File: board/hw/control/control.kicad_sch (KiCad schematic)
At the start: 25 parts, among them J1 stepper #1, J2 stepper #2, J3 buttons, J4 power, J6 AVR-ISP-10, U1 ULN2003A, U2 ULN2003A, U3 ULN2003A, U4 ULN2003A, U5 LM78L05_SO8

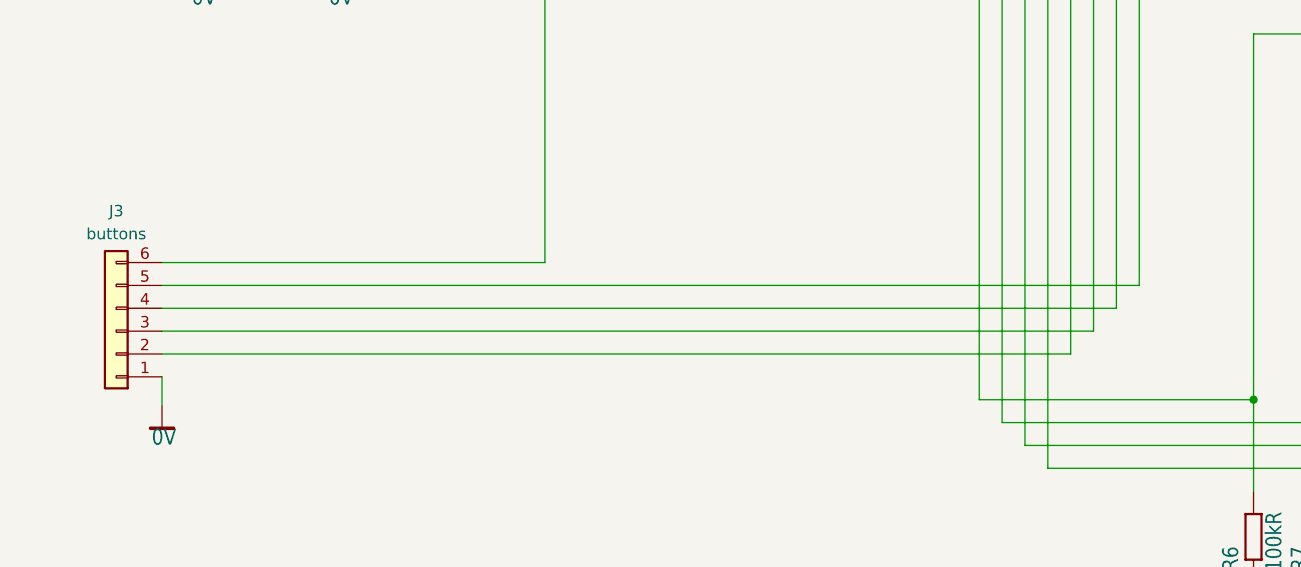
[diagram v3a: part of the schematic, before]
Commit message: assigned correct sizes of elements + some draft positioning; still need to add power management cirtcuitry
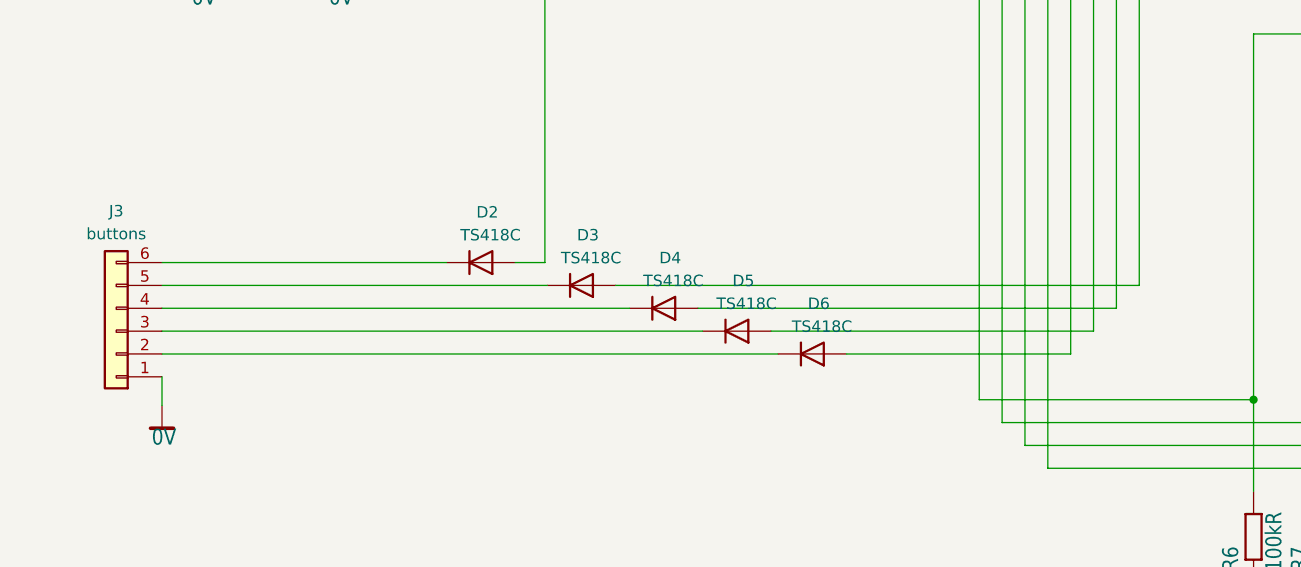
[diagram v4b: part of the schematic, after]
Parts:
- added D2, D3, D4, D5, D6: TS418C, Diode_SMD:D_0805_2012Metric, symbol Diode:CD4148W
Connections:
- net at J3.2 (Pin_2): now also D6.1 (K); no longer U$1.8 ((T0)PD4)
- net at J3.3 (Pin_3): now also D5.1 (K); no longer U$1.9 ((T1)PD5)
- net at J3.4 (Pin_4): now also D4.1 (K); no longer U$1.11 ((ICP)PD6)
- net at J3.5 (Pin_5): now also D3.1 (K); no longer U$1.16 ((OC1B)PB4)
- net at J3.6 (Pin_6): now also D2.1 (K); no longer U$1.5 (PA0(XTAL1))
- new net: D3.2 (A), U$1.16 ((OC1B)PB4)
- new net: D6.2 (A), U$1.8 ((T0)PD4)
- new net: D2.2 (A), U$1.5 (PA0(XTAL1))
- new net: D4.2 (A), U$1.11 ((ICP)PD6)
- new net: D5.2 (A), U$1.9 ((T1)PD5)
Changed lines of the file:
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@@
+    (stroke (width 0) (type default))
+  )
+  (wire (pts (xy 77.978 142.24) (xy 81.28 142.24))
     (stroke (width 0) (type default))
   )
@@
     (stroke (width 0) (type default))
   )
+  (wire (pts (xy 89.154 144.78) (xy 147.32 144.78))
+    (stroke (width 0) (type default))
+  )
   (wire (pts (xy 240.03 81.28) (xy 246.38 81.28))
     (stroke (width 0) (type default))
@@
     (stroke (width 0) (type default))
   )
+  (wire (pts (xy 114.808 152.4) (xy 139.7 152.4))
+    (stroke (width 0) (type default))
+  )
   (wire (pts (xy 257.81 116.84) (xy 245.11 116.84))
     (stroke (width 0) (type default))
@@
     (stroke (width 0) (type default))
   )
+  (wire (pts (xy 106.426 149.86) (xy 142.24 149.86))
+    (stroke (width 0) (type default))
+  )
   (wire (pts (xy 88.9 88.9) (xy 81.28 88.9))
     (stroke (width 0) (type default))
@@
     (stroke (width 0) (type default))
   )
+  (wire (pts (xy 38.735 144.78) (xy 81.534 144.78))
+    (stroke (width 0) (type default))
+  )
   (wire (pts (xy 160.02 167.64) (xy 160.02 157.48))
     (stroke (width 0) (type default))
@@
     (stroke (width 0) (type default))
   )
+  (wire (pts (xy 38.735 142.24) (xy 70.358 142.24))
+    (stroke (width 0) (type default))
+  )
   (wire (pts (xy 213.36 116.84) (xy 160.02 116.84))
     (stroke (width 0) (type default))
@@
     (stroke (width 0) (type default))
   )
-  (wire (pts (xy 38.735 144.78) (xy 147.32 144.78))
-    (stroke (width 0) (type default))
-  )
   (wire (pts (xy 38.735 154.94) (xy 38.735 158.115))
     (stroke (width 0) (type default))
@@
     (stroke (width 0) (type default))
   )
-  (wire (pts (xy 38.735 152.4) (xy 139.7 152.4))
-    (stroke (width 0) (type default))
-  )
   (wire (pts (xy 213.36 127) (xy 213.36 129.54))
     (stroke (width 0) (type default))
@@
     (stroke (width 0) (type default))
   )
+  (wire (pts (xy 98.298 147.32) (xy 144.78 147.32))
+    (stroke (width 0) (type default))
+  )
   (wire (pts (xy 147.32 71.12) (xy 147.32 144.78))
     (stroke (width 0) (type default))
@@
     (stroke (width 0) (type default))
   )
-  (wire (pts (xy 38.735 147.32) (xy 144.78 147.32))
-    (stroke (width 0) (type default))
-  )
   (wire (pts (xy 213.36 76.2) (xy 185.42 76.2))
     (stroke (width 0) (type default))
   )
-  (wire (pts (xy 38.735 149.86) (xy 142.24 149.86))
-    (stroke (width 0) (type default))
-  )
   (wire (pts (xy 219.71 119.38) (xy 213.36 119.38))
     (stroke (width 0) (type default))
@@
     (stroke (width 0) (type default))
   )
+  (wire (pts (xy 38.735 152.4) (xy 107.188 152.4))
+    (stroke (width 0) (type default))
+  )
   (wire (pts (xy 127 63.5) (xy 134.874 63.5))
     (stroke (width 0) (type default))
@@
     (stroke (width 0) (type default))
   )
-  (wire (pts (xy 38.735 142.24) (xy 81.28 142.24))
-    (stroke (width 0) (type default))
-  )
   (wire (pts (xy 213.36 167.64) (xy 213.36 170.18))
     (stroke (width 0) (type default))
@@
     (stroke (width 0) (type default))
   )
+  (wire (pts (xy 38.735 149.86) (xy 98.806 149.86))
+    (stroke (width 0) (type default))
+  )
   (wire (pts (xy 132.08 160.02) (xy 167.64 160.02))
     (stroke (width 0) (type default))
@@
     (stroke (width 0) (type default))
   )
+  (wire (pts (xy 38.735 147.32) (xy 90.678 147.32))
+    (stroke (width 0) (type default))
+  )
   (wire (pts (xy 219.71 83.82) (xy 219.71 90.17))
     (stroke (width 0) (type default))
@@
     )
   )
+  (symbol (lib_id "Diode:CD4148W") (at 85.344 144.78 0) (mirror x) (unit 1)
+    (in_bom yes) (on_board yes) (dnp no)
+    (property "Reference" "D3" (at 84.836 139.192 0)
+      (effects (font (size 1.27 1.27)) (justify left))
+    )
+    (property "Value" "TS418C" (at 83.058 141.732 0)
+      (effects (font (size 1.27 1.27)) (justify left))
+    )
+    (property "Footprint" "Diode_SMD:D_0805_2012Metric" (at 85.344 139.7 0)
+      (effects (font (size 1.27 1.27)) hide)
+    )
+    (property "Datasheet" "https://www.dccomponents.com/upload/product/original/623524775088.pdf" (at 85.344 144.78 0)
+      (effects (font (size 1.27 1.27)) hide)
+    )
+    (property "Sim.Device" "D" (at 85.344 144.78 0)
+      (effects (font (size 1.27 1.27)) hide)
+    )
+    (property "Sim.Pins" "1=K 2=A" (at 85.344 144.78 0)
+      (effects (font (size 1.27 1.27)) hide)
+    )
+    (pin "1")
+    (pin "2")
+    (instances
+      (project "control"
+        (path "/99b3aba4-a2cc-4425-a477-43f3a410d922"
+          (reference "D3") (unit 1)
+        )
+      )
+    )
+  )
   (symbol (lib_id "control-eagle-import:0V") (at 58.42 111.76 0) (unit 1)
     (in_bom yes) (on_board yes) (dnp no)
@@
         (path "/99b3aba4-a2cc-4425-a477-43f3a410d922"
           (reference "#SUPPLY027") (unit 1)
+        )
+      )
+    )
+  )
+  (symbol (lib_id "Diode:CD4148W") (at 110.998 152.4 0) (mirror x) (unit 1)
+    (in_bom yes) (on_board yes) (dnp no)
+    (property "Reference" "D6" (at 110.49 146.812 0)
+      (effects (font (size 1.27 1.27)) (justify left))
+    )
+    (property "Value" "TS418C" (at 108.712 149.352 0)
+      (effects (font (size 1.27 1.27)) (justify left))
+    )
+    (property "Footprint" "Diode_SMD:D_0805_2012Metric" (at 110.998 147.32 0)
+      (effects (font (size 1.27 1.27)) hide)
+    )
+    (property "Datasheet" "https://www.dccomponents.com/upload/product/original/623524775088.pdf" (at 110.998 152.4 0)
+      (effects (font (size 1.27 1.27)) hide)
+    )
+    (property "Sim.Device" "D" (at 110.998 152.4 0)
+      (effects (font (size 1.27 1.27)) hide)
+    )
+    (property "Sim.Pins" "1=K 2=A" (at 110.998 152.4 0)
+      (effects (font (size 1.27 1.27)) hide)
+    )
+    (pin "1")
+    (pin "2")
+    (instances
+      (project "control"
+        (path "/99b3aba4-a2cc-4425-a477-43f3a410d922"
+          (reference "D6") (unit 1)
         )
       )
@@
     )
   )
+  (symbol (lib_id "Diode:CD4148W") (at 74.168 142.24 0) (mirror x) (unit 1)
+    (in_bom yes) (on_board yes) (dnp no)
+    (property "Reference" "D2" (at 73.66 136.652 0)
+      (effects (font (size 1.27 1.27)) (justify left))
+    )
+    (property "Value" "TS418C" (at 71.882 139.192 0)
+      (effects (font (size 1.27 1.27)) (justify left))
+    )
+    (property "Footprint" "Diode_SMD:D_0805_2012Metric" (at 74.168 137.16 0)
+      (effects (font (size 1.27 1.27)) hide)
+    )
+    (property "Datasheet" "https://www.dccomponents.com/upload/product/original/623524775088.pdf" (at 74.168 142.24 0)
+      (effects (font (size 1.27 1.27)) hide)
+    )
+    (property "Sim.Device" "D" (at 74.168 142.24 0)
+      (effects (font (size 1.27 1.27)) hide)
+    )
+    (property "Sim.Pins" "1=K 2=A" (at 74.168 142.24 0)
+      (effects (font (size 1.27 1.27)) hide)
+    )
+    (pin "1")
+    (pin "2")
+    (instances
+      (project "control"
+        (path "/99b3aba4-a2cc-4425-a477-43f3a410d922"
+          (reference "D2") (unit 1)
+        )
+      )
+    )
+  )
   (symbol (lib_id "power:+24V") (at 261.62 132.08 0) (unit 1)
     (in_bom yes) (on_board yes) (dnp no)
@@
         (path "/99b3aba4-a2cc-4425-a477-43f3a410d922"
           (reference "C6") (unit 1)
+        )
+      )
+    )
+  )
+  (symbol (lib_id "Diode:CD4148W") (at 94.488 147.32 0) (mirror x) (unit 1)
+    (in_bom yes) (on_board yes) (dnp no)
+    (property "Reference" "D4" (at 93.98 141.732 0)
+      (effects (font (size 1.27 1.27)) (justify left))
+    )
+    (property "Value" "TS418C" (at 92.202 144.272 0)
+      (effects (font (size 1.27 1.27)) (justify left))
+    )
+    (property "Footprint" "Diode_SMD:D_0805_2012Metric" (at 94.488 142.24 0)
+      (effects (font (size 1.27 1.27)) hide)
+    )
+    (property "Datasheet" "https://www.dccomponents.com/upload/product/original/623524775088.pdf" (at 94.488 147.32 0)
+      (effects (font (size 1.27 1.27)) hide)
+    )
+    (property "Sim.Device" "D" (at 94.488 147.32 0)
+      (effects (font (size 1.27 1.27)) hide)
+    )
+    (property "Sim.Pins" "1=K 2=A" (at 94.488 147.32 0)
+      (effects (font (size 1.27 1.27)) hide)
+    )
+    (pin "1")
+    (pin "2")
+    (instances
+      (project "control"
+        (path "/99b3aba4-a2cc-4425-a477-43f3a410d922"
+          (reference "D4") (unit 1)
         )
       )
@@
         )
       )
+    )
+  )
+  (symbol (lib_id "Diode:CD4148W") (at 102.616 149.86 0) (mirror x) (unit 1)
+    (in_bom yes) (on_board yes) (dnp no)
+    (property "Reference" "D5" (at 102.108 144.272 0)
+      (effects (font (size 1.27 1.27)) (justify left))
+    )
+    (property "Value" "TS418C" (at 100.33 146.812 0)
+      (effects (font (size 1.27 1.27)) (justify left))
+    )
+    (property "Footprint" "Diode_SMD:D_0805_2012Metric" (at 102.616 144.78 0)
+      (effects (font (size 1.27 1.27)) hide)
+    )
+    (property "Datasheet" "https://www.dccomponents.com/upload/product/original/623524775088.pdf" (at 102.616 149.86 0)
+      (effects (font (size 1.27 1.27)) hide)
+    )
+    (property "Sim.Device" "D" (at 102.616 149.86 0)
+      (effects (font (size 1.27 1.27)) hide)
+    )
+    (property "Sim.Pins" "1=K 2=A" (at 102.616 149.86 0)
+      (effects (font (size 1.27 1.27)) hide)
+    )
+    (pin "1")
+    (pin "2")
+    (instances
+      (project "control"
+        (path "/99b3aba4-a2cc-4425-a477-43f3a410d922"
+          (reference "D5") (unit 1)
+        )
+      )

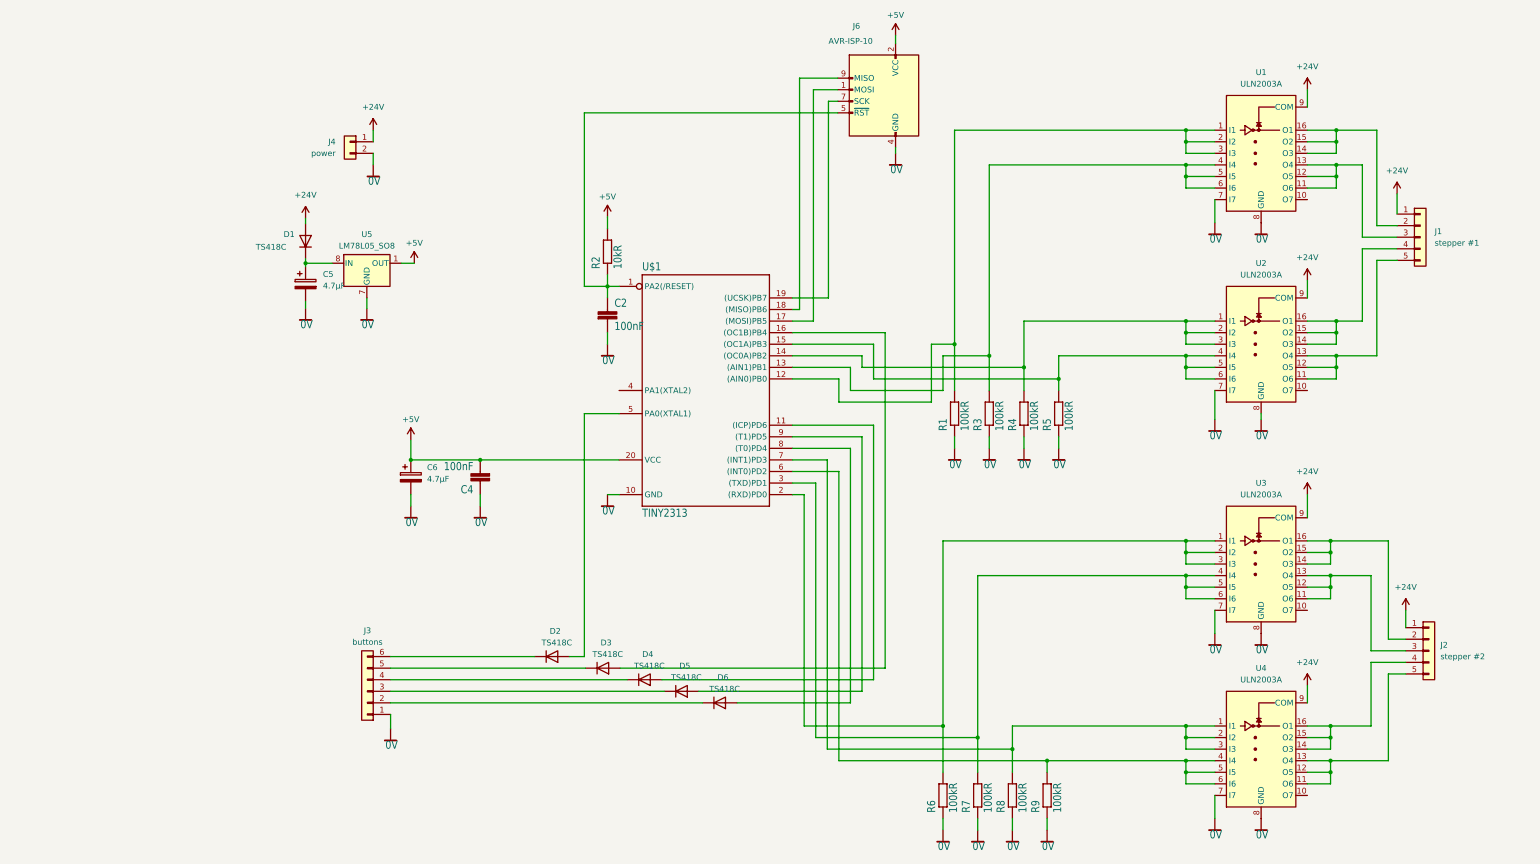
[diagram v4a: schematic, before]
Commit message: added p-mosfet and zerenrs for power ctrl via buttons, too
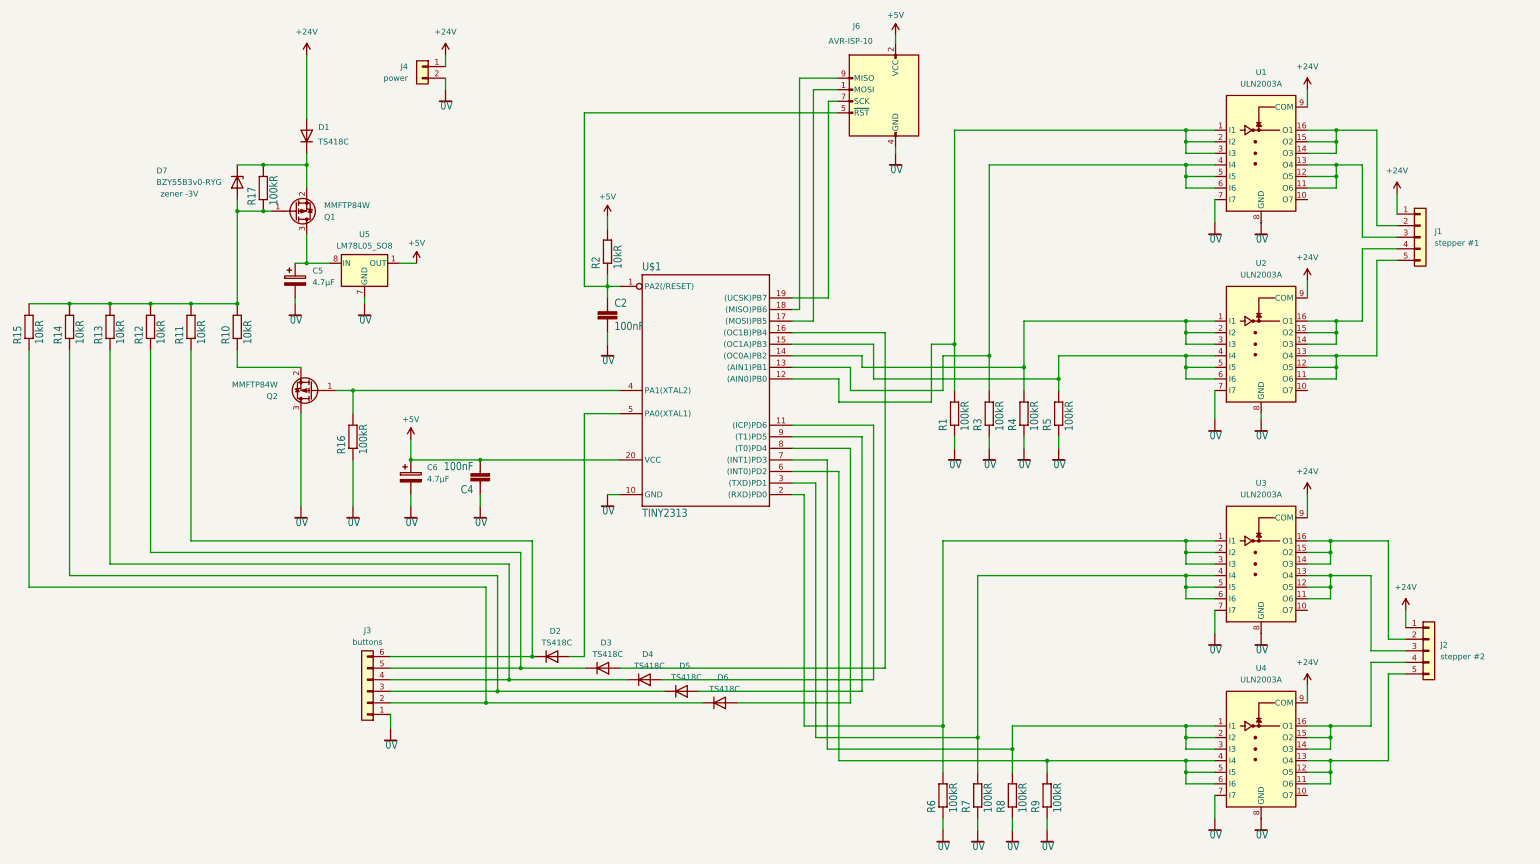
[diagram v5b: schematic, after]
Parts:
- added D7: BZY55B3v0-RYG, Diode_SMD:D_0805_2012Metric_Pad1.15x1.40mm_HandSolder, symbol Device:D_Zener
- added Q1, Q2: MMFTP84W, Package_TO_SOT_SMD:SOT-323_SC-70, symbol Device:Q_PMOS_GSD
- added R10, R11, R12, R13, R14, R15: 10kR, Resistor_SMD:R_0805_2012Metric_Pad1.20x1.40mm_HandSolder, symbol control-eagle-import:R-EU_MELF0204W
- added R16, R17: 100kR, Resistor_SMD:R_0805_2012Metric_Pad1.20x1.40mm_HandSolder, symbol control-eagle-import:R-EU_MELF0204W
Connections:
- net 0V: now also Q2.3 (D), R16.1
- net at D3.1 (K), J3.5 (Pin_5): now also R12.1
- net at D6.1 (K), J3.2 (Pin_2): now also R15.1
- net at C5.1, U5.8 (IN): now also Q1.3 (D); no longer D1.1 (K)
- net at D2.1 (K), J3.6 (Pin_6): now also R11.1
- net at D4.1 (K), J3.4 (Pin_4): now also R13.1
- net at D5.1 (K), J3.3 (Pin_3): now also R14.1
- net at U$1.4 (PA1(XTAL2)): now also Q2.1 (G), R16.2
- new net: D7.2 (A), Q1.1 (G), R10.2, R11.2, R12.2, R13.2, R14.2, R15.2, R17.1
- new net: D1.1 (K), D7.1 (K), Q1.2 (S), R17.2
- new net: Q2.2 (S), R10.1
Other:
- moved on the sheet: C5, D1, J4, U5
